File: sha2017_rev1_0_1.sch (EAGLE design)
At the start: 201 parts, among them IC1 CP210X_USB_UART, IC2 LD117AS33TR, IC3 ESP32WROOM32, IC4 TP4056, M1 MOTOR10MM, Q1 MMBT2222A, Q2 MMBT2222A, Q3 MMBT2222A, Q4 MMBT2222A, Q5 SI1304 BDL, Q6 MMBT2222A, T1 MOSFET-PCHANNEL, T2 MOSFET-PCHANNEL, T3 MOSFET-PCHANNEL, U1 MPR121QR2, X2 2908-05WB-MG, X4 JST-PH3

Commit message: Add option for GD/DKE displays - TODO: ROUTE
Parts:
- added C42: 1u, sha2017_rev0_1_0_dev:C0603-DASHES
- added R26: 0R, sha2017_rev0_1_0_dev:R0603-DASHES
- L1: value 22µ -> 47µ
- R19: value 5R -> 2R7
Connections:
- new net LCD_VDD: C42.1, R26.2, X1.7
- net +3V3: now also R26.1; no longer X1.7
- net GND: now also C42.2
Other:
- note added: "Model selector: GDEH029A1: Populate R26 DEPG0290B01: Do not populate R26"
- moved on the sheet: C20, C25, C32, C36, D7, D8, D9, L1, Q5, R19

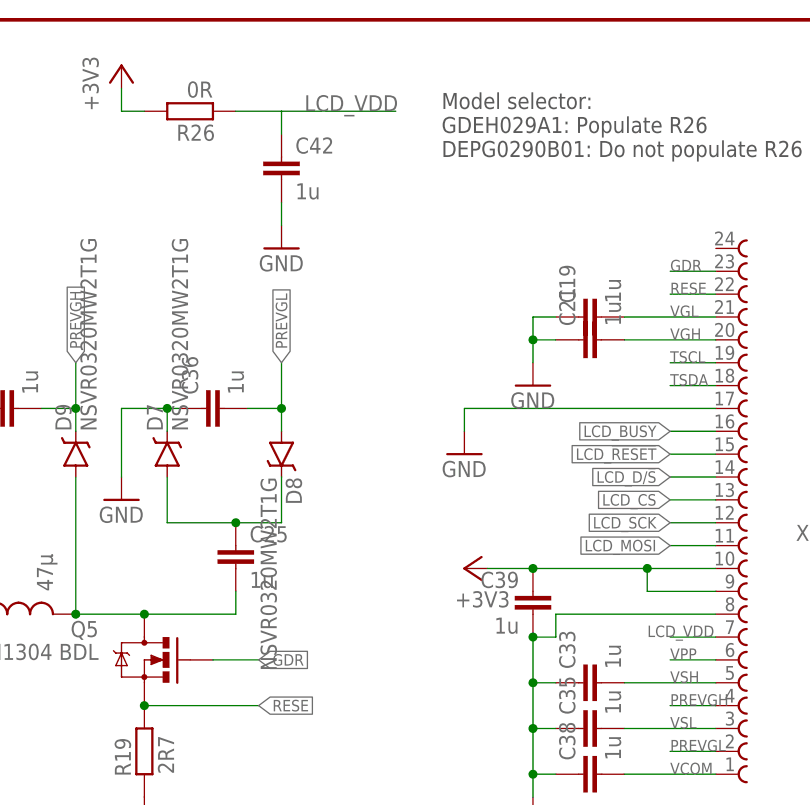
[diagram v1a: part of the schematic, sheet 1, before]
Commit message: routing of display option
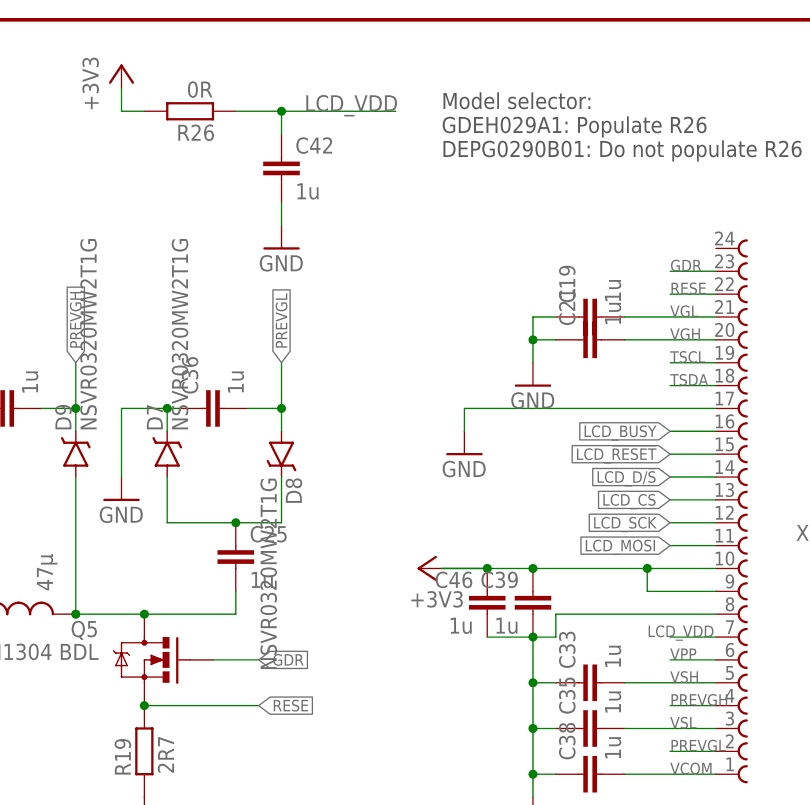
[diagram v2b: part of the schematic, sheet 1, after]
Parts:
- added C46: 1u, sha2017_rev0_1_0_dev:C0603-DASHES
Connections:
- net +3V3: now also C46.1
- net GND: now also C46.2
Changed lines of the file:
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@@
 <part name="+3V11" library="supply1" deviceset="+3V3" device=""/>
 <part name="GND36" library="supply1" deviceset="GND" device=""/>
+<part name="C46" library="sha2017_rev0_1_0_dev" deviceset="C0603-DASHES" device="" value="1u">
+<attribute name="PARTNO" value="GRM188R61E105KA12D"/>
+</part>
 </parts>
 <sheets>
@@
 <instance part="GND34" gate="1" x="345.44" y="213.36"/>
 <instance part="GND35" gate="1" x="337.82" y="205.74"/>
-<instance part="+3V1" gate="G$1" x="337.82" y="193.04" rot="R90"/>
+<instance part="+3V1" gate="G$1" x="332.74" y="193.04" rot="R90"/>
 <instance part="C39" gate="G$1" x="345.44" y="189.23" rot="MR0">
 <attribute name="PARTNO" x="345.44" y="189.23" size="1.778" layer="96" rot="MR0" display="off"/>
@@
 <instance part="+3V11" gate="G$1" x="299.72" y="248.92"/>
 <instance part="GND36" gate="1" x="317.5" y="228.6"/>
+<instance part="C46" gate="G$1" x="340.36" y="189.23" rot="MR0">
+<attribute name="PARTNO" x="340.36" y="189.23" size="1.778" layer="96" rot="MR0" display="off"/>
+</instance>
 </instances>
 <busses>
@@
 <junction x="345.44" y="185.42"/>
 <junction x="345.44" y="180.34"/>
+<pinref part="C46" gate="G$1" pin="2"/>
+<wire x1="340.36" y1="185.42" x2="345.44" y2="185.42" width="0.1524" layer="91"/>
 </segment>
 <segment>
@@
 <junction x="345.44" y="193.04"/>
 <wire x1="345.44" y1="193.04" x2="340.36" y2="193.04" width="0.1524" layer="91"/>
+<pinref part="C46" gate="G$1" pin="1"/>
+<wire x1="340.36" y1="193.04" x2="335.28" y2="193.04" width="0.1524" layer="91"/>
+<wire x1="335.28" y1="193.04" x2="340.36" y2="193.04" width="0.1524" layer="91"/>
+<junction x="340.36" y="193.04"/>
 </segment>
 <segment>
@@
 <wire x1="317.5" y1="243.84" x2="330.2" y2="243.84" width="0.1524" layer="91"/>
 <label x="320.04" y="243.84" size="1.778" layer="95"/>
-</segment>
-</net>
+<junction x="317.5" y="243.84"/>
+</segment>
+</net>

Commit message: FINAL gerbers, design freeze
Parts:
- F1, F2: value 900mA -> 1A
- IC2: value LD117AS33TR -> AP2114H
- R30: value 0R27 -> 0R27 1/4W
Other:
- note added: "SHA2017 Badge"
- note added: "SK6812 RGBW (5050 package)"
- note removed: "WS2812"
- moved on the sheet: C14, C15, C17, C18, C22, C26, C27, C30, IC2
